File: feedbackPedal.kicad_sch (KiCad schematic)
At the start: 61 parts, among them J1 power, J2 send, J3 input, J4 output, J5 return, J6 footswitch, J7 mech_fs, K2 FTR-B4CB4.5Z, SW1 LIM_ON, SW2 PHASE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

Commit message: made some attiny tweaks
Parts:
- added R22: 10K, Resistor_SMD:R_0603_1608Metric, symbol Device:R
- R20: value 75R -> 470R
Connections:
- net 5V: now also R22.1
- net at U5.1 (~{RESET}/PB5): now also R22.2
- no-connect marks 9 -> 8
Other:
- note added: "PUT A TVS HERE!! something like a SMF5.0CA - part C364279 on lcsc"

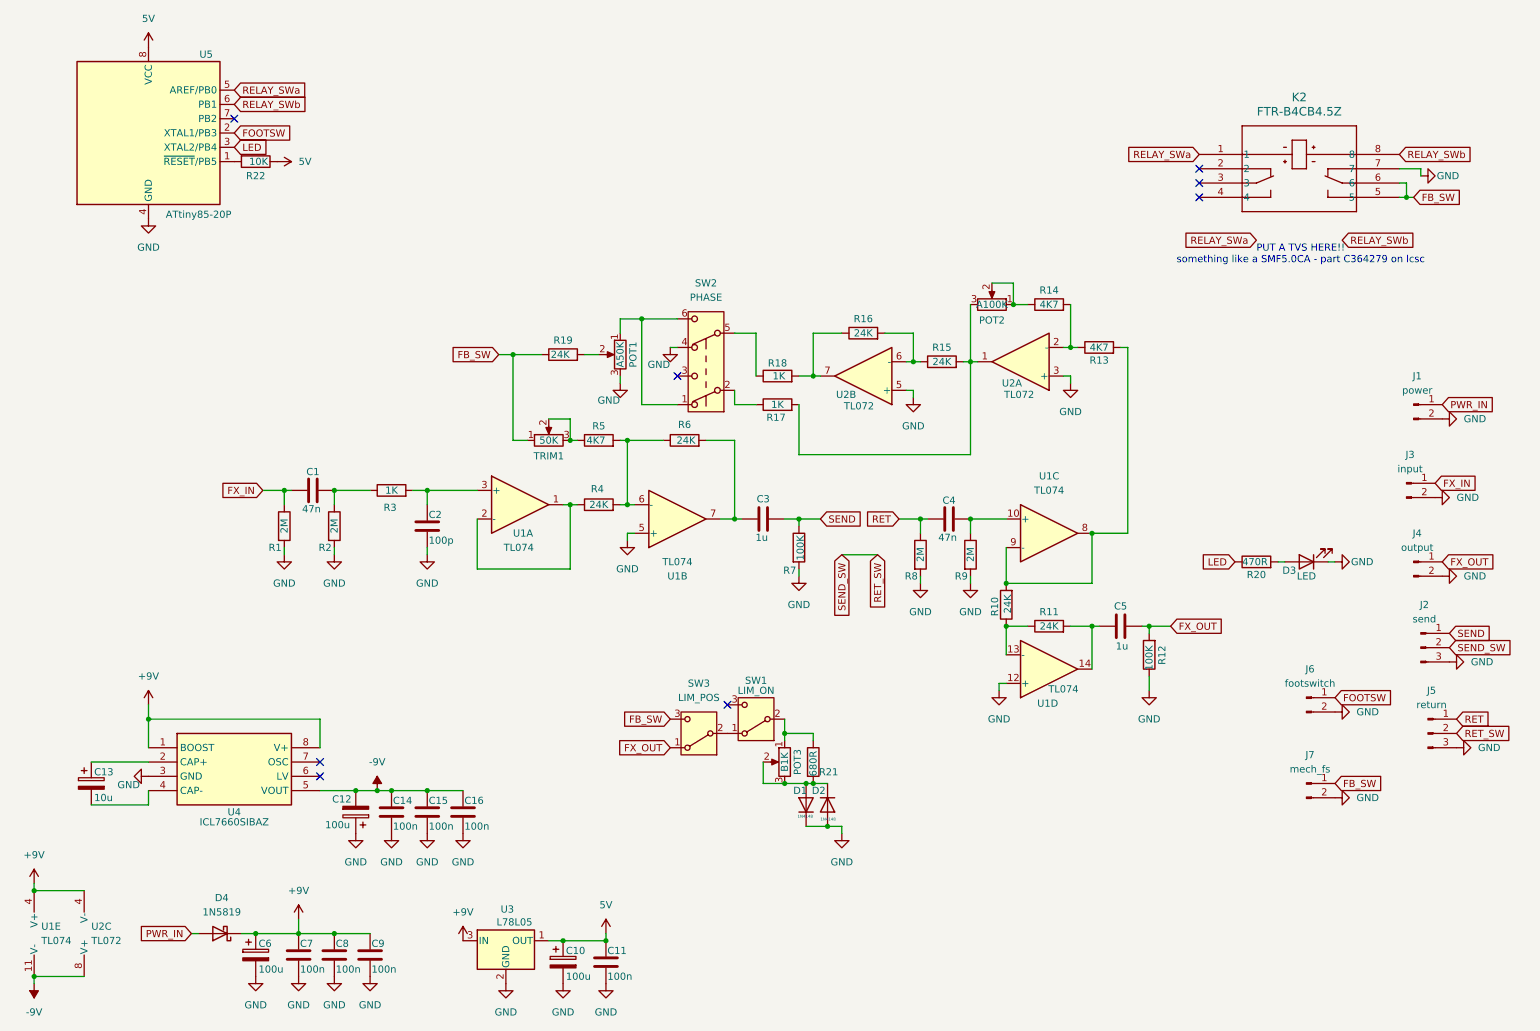
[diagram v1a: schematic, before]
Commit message: replace attiny & relay with ch32 and analogue switch
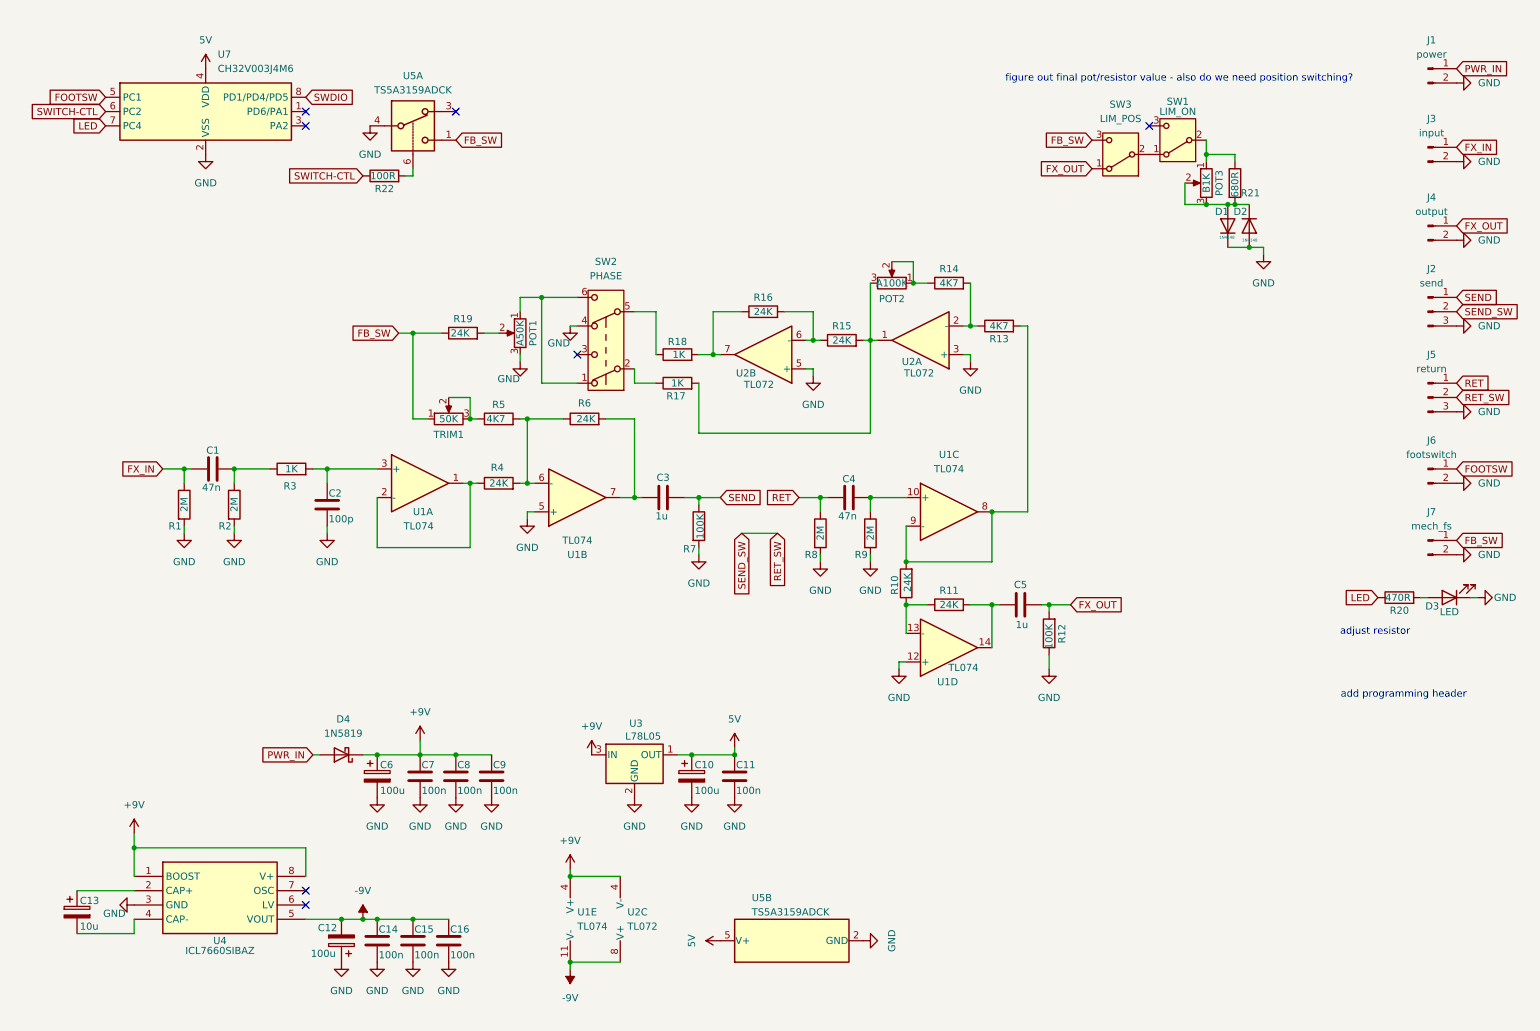
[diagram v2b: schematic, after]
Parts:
- removed K2: FTR-B4CB4.5Z, footprints:FTR-B4C_FUJ, symbol 2024-11-10_10-40-11:FTR-B4CB4.5Z
- removed U5: ATtiny85-20P, Package_DIP:DIP-8_W7.62mm, symbol MCU_Microchip_ATtiny:ATtiny85-20P
- added U5: TS5A3159ADCK, Package_TO_SOT_SMD:SOT-363_SC-70-6, symbol Analog_Switch:TS5A3159ADCK
- added U7: CH32V003J4M6, Package_SO:JEITA_SOIC-8_3.9x4.9mm_P1.27mm, symbol MCU_WCH_RiscV:CH32V003JxMx
- R22: value 10K -> 100R
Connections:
- net 5V: now also U5.5 (V+), U7.4 (VDD); no longer R22.1
- net FB_SW: now also U5.1
- net FOOTSW: now also U7.5 (PC1)
- net GND: now also U5.2 (GND), U5.4, U7.2 (VSS)
- net LED: now also U7.7 (PC4)
- net at R22.2: now also U5.6
- new net SWDIO: U7.8 (PD1/PD4/PD5)
- new net SWITCH-CTL: R22.1, U7.6 (PC2)
- no-connect marks 8 -> 7
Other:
- note added: "add programming header"
- note added: "adjust resistor"
- note added: "figure out final pot/resistor value - also do we need position switching?"
- note removed: "PUT A TVS HERE!! something like a SMF5.0CA - part C364279 on lcsc"
- moved on the sheet: C1, C10, C11, C12, C13, C14, C15, C16, C2, C3, C4, C5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
